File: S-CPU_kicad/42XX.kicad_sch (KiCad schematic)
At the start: 161 parts, among them U34 OR_2, U35 OR_2, U36 OR_2, U37 OR_2, U6 MUX

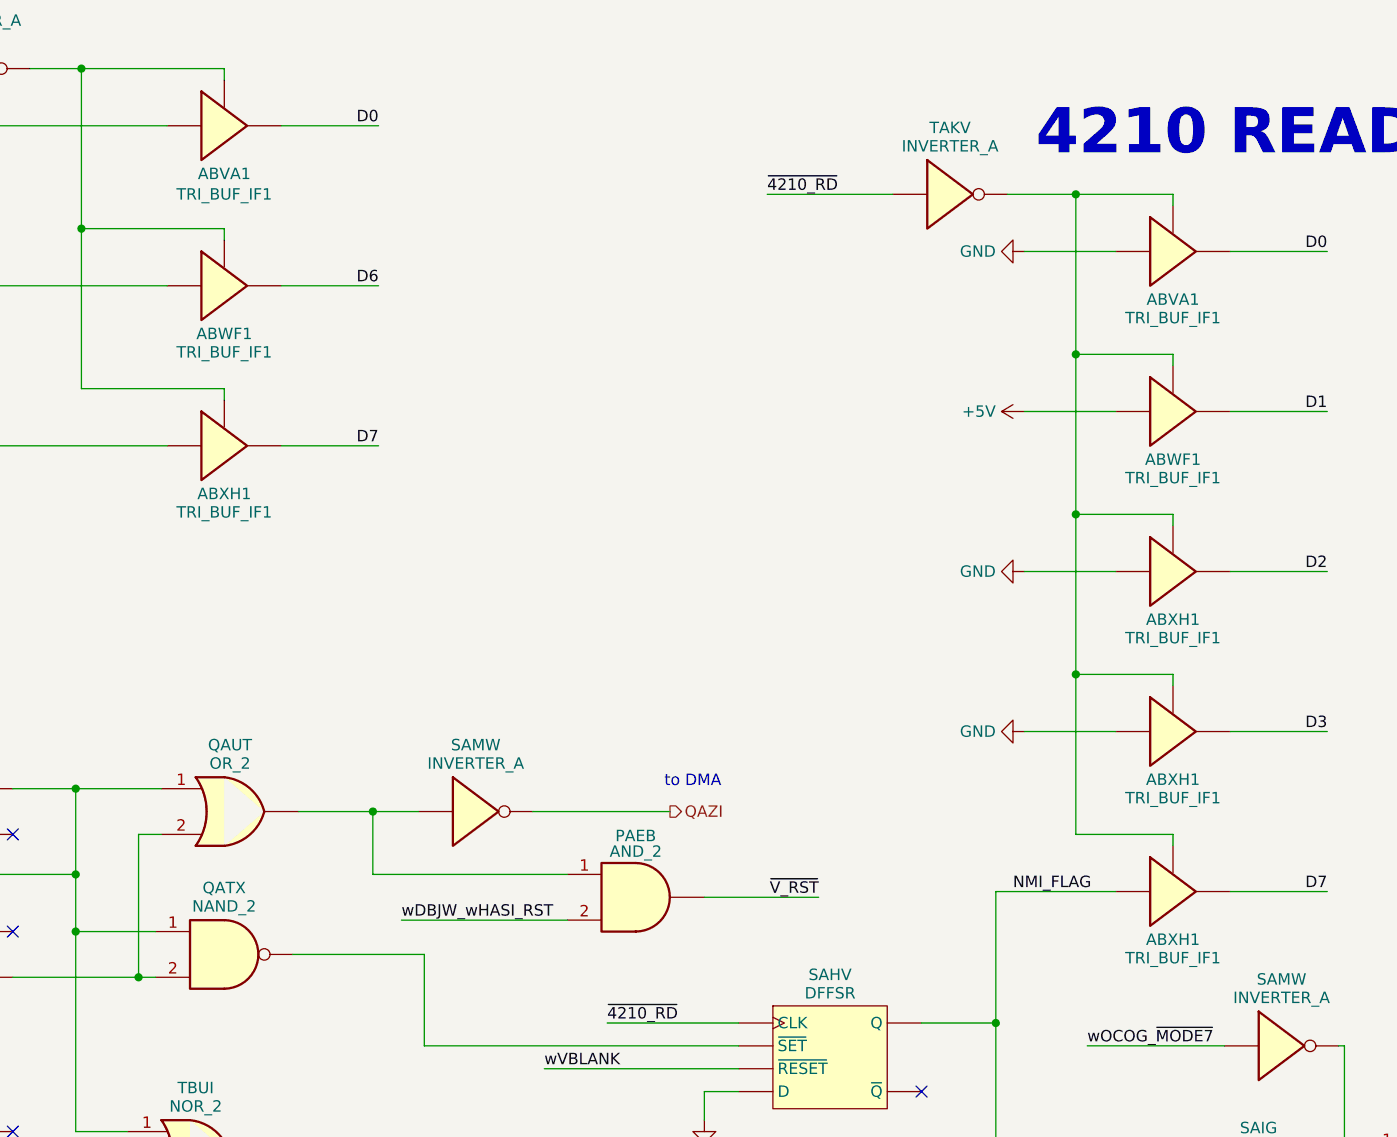
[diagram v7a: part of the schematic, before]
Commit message: Some cells had the wrong ID in the producter remainder sheet. Allocation of new names in spreadsheet for cells in the DMA section
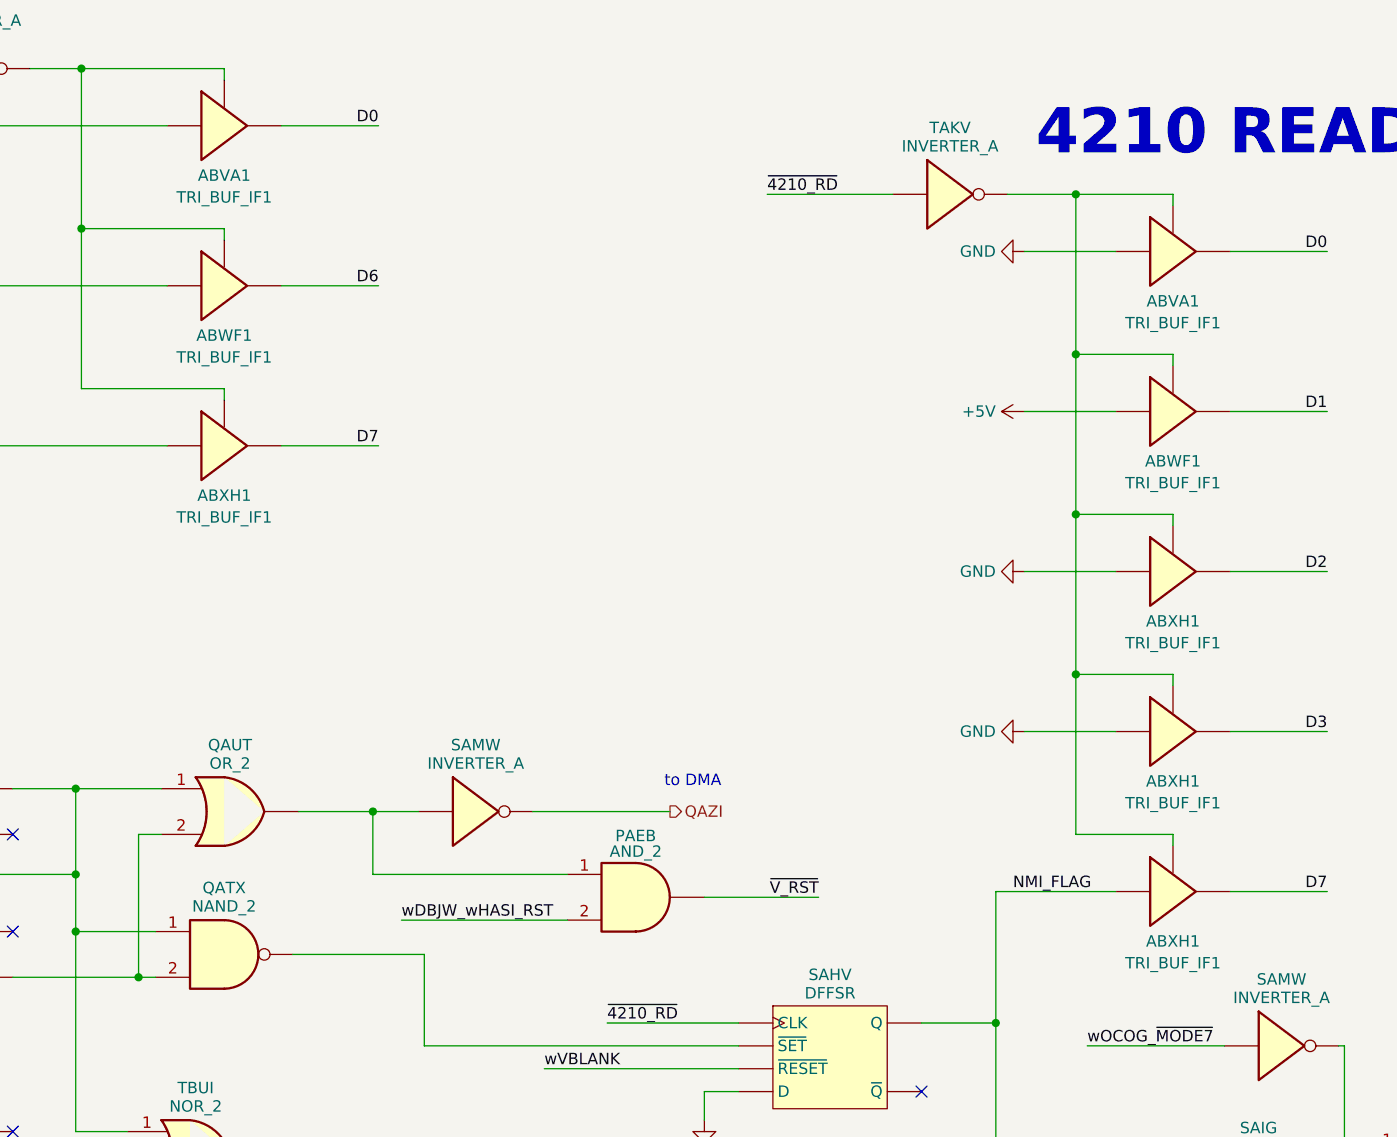
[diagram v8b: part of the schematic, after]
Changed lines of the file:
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@@
   (symbol (lib_id "Ricoh_Cells:TRI_BUF_IF1") (at 454.66 109.22 0) (unit 1)
     (in_bom yes) (on_board yes) (dnp no) (fields_autoplaced)
-    (property "Reference" "ABXH1" (at 454.66 114.562 0)
+    (property "Reference" "ABXH1" (at 454.66 114.7501 0)
       (effects (font (size 1.27 1.27)))
     )
-    (property "Value" "TRI_BUF_IF1" (at 454.66 116.61 0)
+    (property "Value" "TRI_BUF_IF1" (at 454.66 117.1743 0)
       (effects (font (size 1.27 1.27)))
     )
@@
         )
         (path "/ca9d3ca9-0297-4b98-a109-b7c162ccc5c3/4dc5cd9a-499d-4e55-930f-d6021c4e63f2"
-          (reference "TAAM") (unit 1)
+          (reference "TAAD1") (unit 1)
         )
       )
@@
   (symbol (lib_id "Ricoh_Cells:TRI_BUF_IF1") (at 349.25 77.47 0) (unit 1)
     (in_bom yes) (on_board yes) (dnp no) (fields_autoplaced)
-    (property "Reference" "ABWF1" (at 349.25 82.812 0)
+    (property "Reference" "ABWF1" (at 349.25 83.0001 0)
       (effects (font (size 1.27 1.27)))
     )
-    (property "Value" "TRI_BUF_IF1" (at 349.25 84.86 0)
+    (property "Value" "TRI_BUF_IF1" (at 349.25 85.4243 0)
       (effects (font (size 1.27 1.27)))
     )
@@
         )
         (path "/ca9d3ca9-0297-4b98-a109-b7c162ccc5c3/4dc5cd9a-499d-4e55-930f-d6021c4e63f2"
-          (reference "TBAF") (unit 1)
+          (reference "TAXO1") (unit 1)
         )
       )
@@
   (symbol (lib_id "Ricoh_Cells:TRI_BUF_IF1") (at 454.66 73.66 0) (unit 1)
     (in_bom yes) (on_board yes) (dnp no) (fields_autoplaced)
-    (property "Reference" "ABVA1" (at 454.66 79.002 0)
+    (property "Reference" "ABVA1" (at 454.66 79.1901 0)
       (effects (font (size 1.27 1.27)))
     )
-    (property "Value" "TRI_BUF_IF1" (at 454.66 81.05 0)
+    (property "Value" "TRI_BUF_IF1" (at 454.66 81.6143 0)
       (effects (font (size 1.27 1.27)))
     )
@@
         )
         (path "/ca9d3ca9-0297-4b98-a109-b7c162ccc5c3/4dc5cd9a-499d-4e55-930f-d6021c4e63f2"
-          (reference "TAIV") (unit 1)
+          (reference "TAAD3") (unit 1)
         )
       )
@@
   (symbol (lib_id "Ricoh_Cells:TRI_BUF_IF1") (at 349.25 95.25 0) (unit 1)
     (in_bom yes) (on_board yes) (dnp no) (fields_autoplaced)
-    (property "Reference" "ABXH1" (at 349.25 100.592 0)
+    (property "Reference" "ABXH1" (at 349.25 100.7801 0)
       (effects (font (size 1.27 1.27)))
     )
-    (property "Value" "TRI_BUF_IF1" (at 349.25 102.64 0)
+    (property "Value" "TRI_BUF_IF1" (at 349.25 103.2043 0)
       (effects (font (size 1.27 1.27)))
     )
@@
         )
         (path "/ca9d3ca9-0297-4b98-a109-b7c162ccc5c3/4dc5cd9a-499d-4e55-930f-d6021c4e63f2"
-          (reference "TAXO") (unit 1)
+          (reference "TAXO0") (unit 1)
         )
       )
@@
   (symbol (lib_id "Ricoh_Cells:TRI_BUF_IF1") (at 454.66 127 0) (unit 1)
     (in_bom yes) (on_board yes) (dnp no) (fields_autoplaced)
-    (property "Reference" "ABXH1" (at 454.66 132.342 0)
+    (property "Reference" "ABXH1" (at 454.66 132.5301 0)
       (effects (font (size 1.27 1.27)))
     )
-    (property "Value" "TRI_BUF_IF1" (at 454.66 134.39 0)
+    (property "Value" "TRI_BUF_IF1" (at 454.66 134.9543 0)
       (effects (font (size 1.27 1.27)))
     )
@@
         )
         (path "/ca9d3ca9-0297-4b98-a109-b7c162ccc5c3/4dc5cd9a-499d-4e55-930f-d6021c4e63f2"
-          (reference "TAAD") (unit 1)
+          (reference "TAAD0") (unit 1)
         )
       )
@@
   (symbol (lib_id "Ricoh_Cells:TRI_BUF_IF1") (at 454.66 91.44 0) (unit 1)
     (in_bom yes) (on_board yes) (dnp no) (fields_autoplaced)
-    (property "Reference" "ABWF1" (at 454.66 96.782 0)
+    (property "Reference" "ABWF1" (at 454.66 96.9701 0)
       (effects (font (size 1.27 1.27)))
     )
-    (property "Value" "TRI_BUF_IF1" (at 454.66 98.83 0)
+    (property "Value" "TRI_BUF_IF1" (at 454.66 99.3943 0)
       (effects (font (size 1.27 1.27)))
     )
@@
         )
         (path "/ca9d3ca9-0297-4b98-a109-b7c162ccc5c3/4dc5cd9a-499d-4e55-930f-d6021c4e63f2"
-          (reference "TAHS") (unit 1)
+          (reference "TAAD2") (unit 1)
         )
       )
@@
   (symbol (lib_id "Ricoh_Cells:TRI_BUF_IF1") (at 454.66 144.78 0) (unit 1)
     (in_bom yes) (on_board yes) (dnp no) (fields_autoplaced)
-    (property "Reference" "ABXH1" (at 454.66 150.122 0)
+    (property "Reference" "ABXH1" (at 454.66 150.3101 0)
       (effects (font (size 1.27 1.27)))
     )
-    (property "Value" "TRI_BUF_IF1" (at 454.66 152.17 0)
+    (property "Value" "TRI_BUF_IF1" (at 454.66 152.7343 0)
       (effects (font (size 1.27 1.27)))
     )
@@
         )
         (path "/ca9d3ca9-0297-4b98-a109-b7c162ccc5c3/4dc5cd9a-499d-4e55-930f-d6021c4e63f2"
-          (reference "TAKJ") (unit 1)
+          (reference "TAAD4") (unit 1)
         )
       )
@@
   (symbol (lib_id "Ricoh_Cells:TRI_BUF_IF1") (at 349.25 59.69 0) (unit 1)
     (in_bom yes) (on_board yes) (dnp no) (fields_autoplaced)
-    (property "Reference" "ABVA1" (at 349.25 65.032 0)
+    (property "Reference" "ABVA1" (at 349.25 65.2201 0)
       (effects (font (size 1.27 1.27)))
     )
-    (property "Value" "TRI_BUF_IF1" (at 349.25 67.31 0)
+    (property "Value" "TRI_BUF_IF1" (at 349.25 67.6443 0)
       (effects (font (size 1.27 1.27)))
     )
@@
         )
         (path "/ca9d3ca9-0297-4b98-a109-b7c162ccc5c3/4dc5cd9a-499d-4e55-930f-d6021c4e63f2"
-          (reference "TBFB") (unit 1)
+          (reference "TAXO2") (unit 1)
         )
       )
